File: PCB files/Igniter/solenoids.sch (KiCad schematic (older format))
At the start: 20 parts, among them Q2 N MOSFET, Q3 N MOSFET, Q4 N MOSFET, Q5 N MOSFET, Q6 N MOSFET

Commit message: 10/26/2019
-Added SD card mounting holes
-Added some more footprints
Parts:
- Q2, Q3, Q4, Q5, Q6: footprint (none) -> Package_TO_SOT_THT:TO-220-3_Horizontal_TabDown
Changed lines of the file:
@@
 F 0 "Q4" H 5276 2846 50  0001 L CNN
 F 1 "N MOSFET" H 5276 2800 50  0000 L CNN
-F 2 "" H 5270 2900 50  0001 C CNN
+F 2 "Package_TO_SOT_THT:TO-220-3_Horizontal_TabDown" H 5270 2900 50  0001 C CNN
 F 3 "~" H 5070 2800 50  0001 C CNN
 	1    5070 2800
@@
 F 0 "Q6" H 7386 2876 50  0001 L CNN
 F 1 "N MOSFET" H 7386 2830 50  0000 L CNN
-F 2 "" H 7380 2930 50  0001 C CNN
+F 2 "Package_TO_SOT_THT:TO-220-3_Horizontal_TabDown" H 7380 2930 50  0001 C CNN
 F 3 "~" H 7180 2830 50  0001 C CNN
 	1    7180 2830
@@
 F 0 "Q5" H 7381 4351 50  0001 L CNN
 F 1 "N MOSFET" H 7381 4305 50  0000 L CNN
-F 2 "" H 7375 4405 50  0001 C CNN
+F 2 "Package_TO_SOT_THT:TO-220-3_Horizontal_TabDown" H 7375 4405 50  0001 C CNN
 F 3 "~" H 7175 4305 50  0001 C CNN
 	1    7175 4305
@@
 F 0 "Q3" H 5271 4321 50  0001 L CNN
 F 1 "N MOSFET" H 5271 4275 50  0000 L CNN
-F 2 "" H 5265 4375 50  0001 C CNN
+F 2 "Package_TO_SOT_THT:TO-220-3_Horizontal_TabDown" H 5265 4375 50  0001 C CNN
 F 3 "~" H 5065 4275 50  0001 C CNN
 	1    5065 4275
@@
 F 0 "Q2" H 5246 5871 50  0001 L CNN
 F 1 "N MOSFET" H 5246 5825 50  0000 L CNN
-F 2 "" H 5240 5925 50  0001 C CNN
+F 2 "Package_TO_SOT_THT:TO-220-3_Horizontal_TabDown" H 5240 5925 50  0001 C CNN
 F 3 "~" H 5040 5825 50  0001 C CNN
 	1    5040 5825

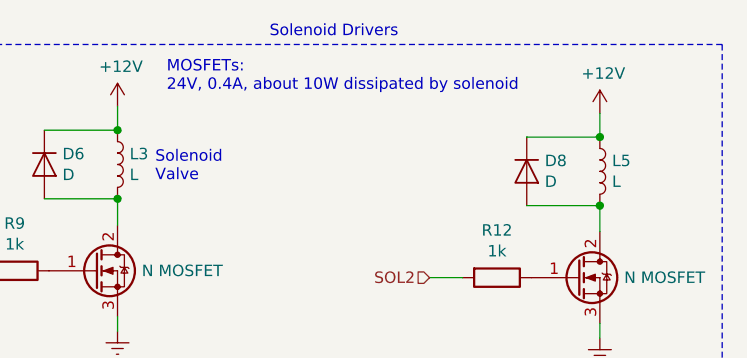
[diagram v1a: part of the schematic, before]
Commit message: 10/27/2019
More 2560 pins named/connected
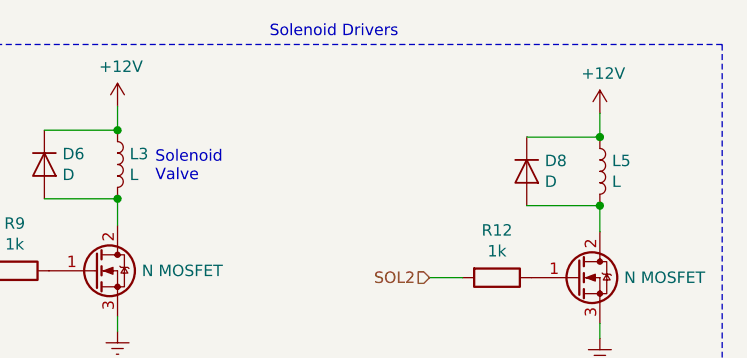
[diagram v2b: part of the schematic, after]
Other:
- note removed: "MOSFETs:\n24V, 0.4A, about 10W dissipated by solenoid\n"
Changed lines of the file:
@@
 LIBS:interface
 LIBS:Igniter-cache
-EELAYER 26 0
+EELAYER 29 0
 EELAYER END
 $Descr A4 11693 8268
@@
 Wire Wire Line
 	7275 4505 7275 4570
-Text Notes 5385 2020 0    50   ~ 0
-MOSFETs:\n24V, 0.4A, about 10W dissipated by solenoid\n
 $Comp
 L Device:Q_NMOS_GDS Q?

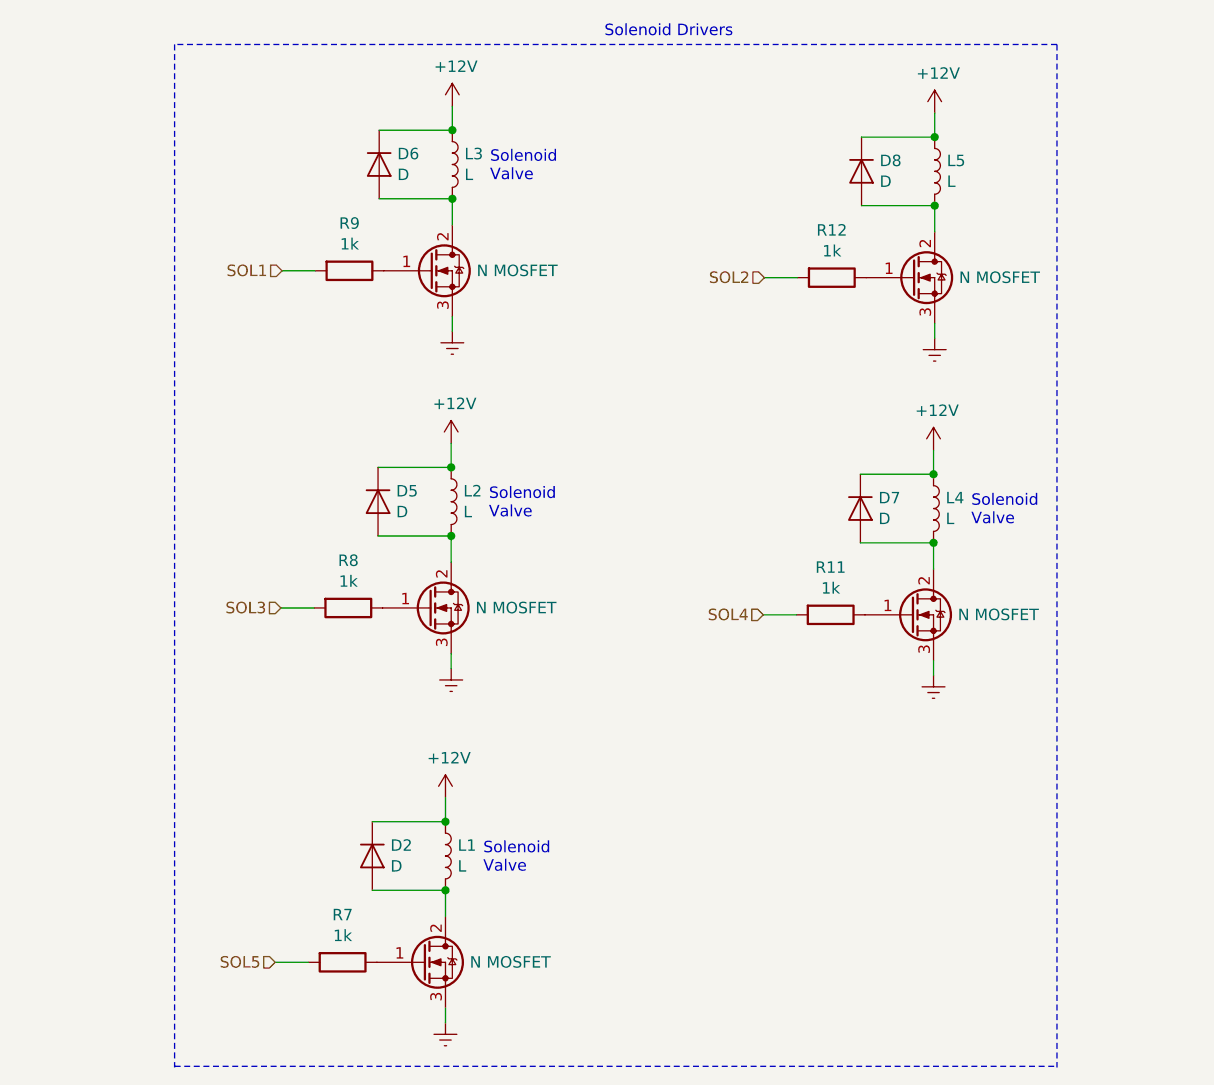
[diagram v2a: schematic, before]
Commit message: 10/30/2019
-Moved keylock
-Removed 1k from MOSFET gates, wasnt adding anything useful to the circuit
-Updated battery voltage to 24V
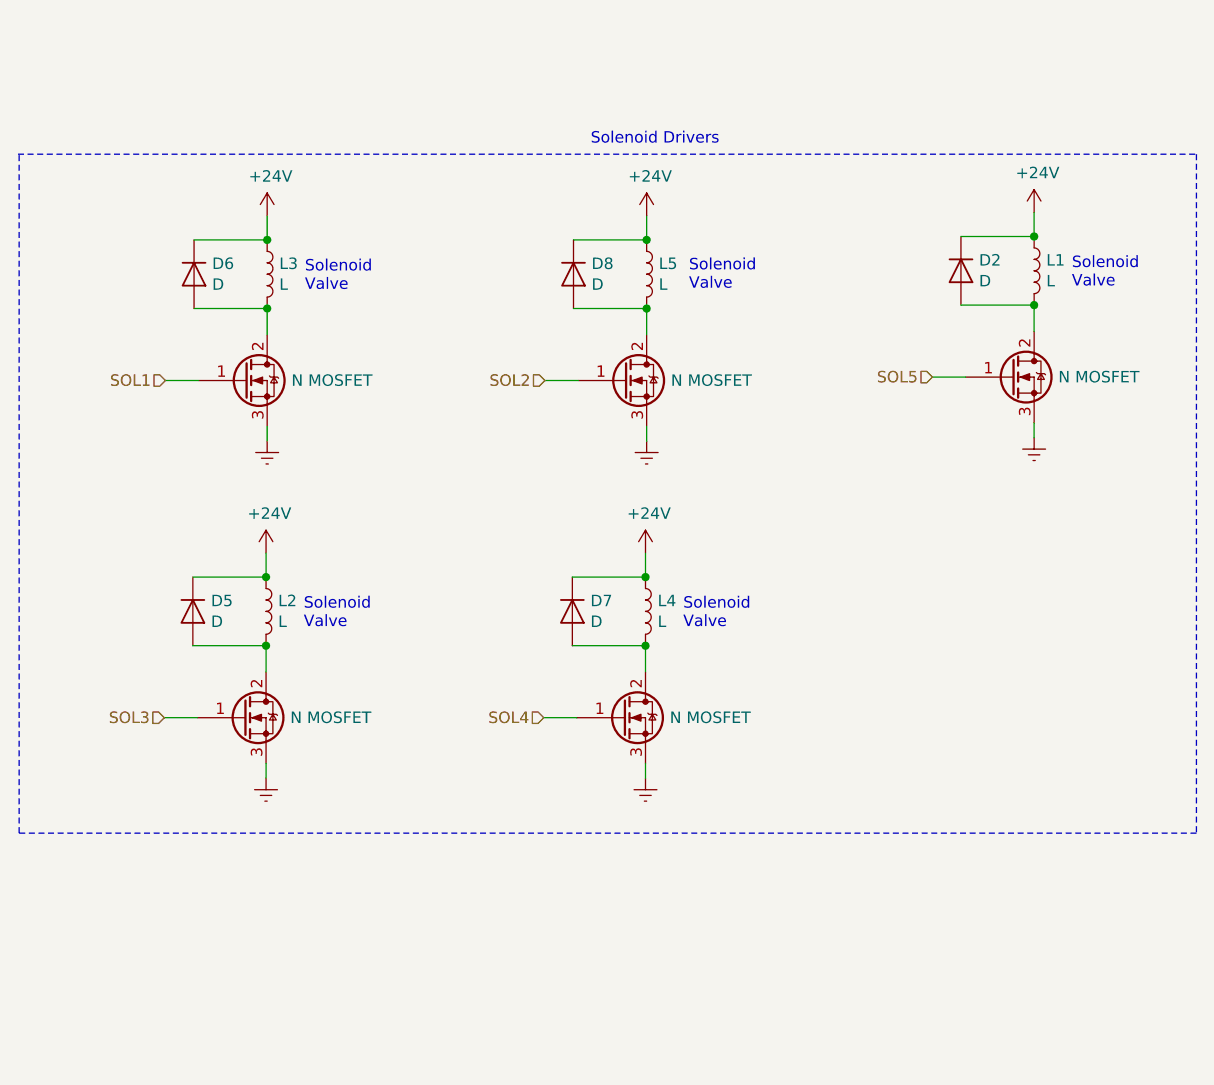
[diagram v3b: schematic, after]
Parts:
- removed R11, R12, R7, R8, R9: 1k, Resistor_THT:R_Axial_DIN0204_L3.6mm_D1.6mm_P5.08mm_Horizontal, symbol Device:R
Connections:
- net SOL1: now also Q4.1 (G)
- net SOL2: now also Q6.1 (G)
- net SOL3: now also Q3.1 (G)
- net SOL4: now also Q5.1 (G)
- net SOL5: now also Q2.1 (G)
- net +12V renamed +24V
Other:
- moved on the sheet: D2, D5, D6, D7, D8, L1, L2, L3, L4, L5

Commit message: 10/31/2019
-Updated and added footprints
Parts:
- D2: footprint (none) -> Diode_THT:D_DO-15_P10.16mm_Horizontal
- D5, D6, D7, D8: footprint (none) -> Diode_THT:D_DO-15_P12.70mm_Horizontal
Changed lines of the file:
@@
 F 0 "D6" V 3994 2894 50  0000 L CNN
 F 1 "D" V 4085 2894 50  0000 L CNN
-F 2 "" H 4040 2815 50  0001 C CNN
+F 2 "Diode_THT:D_DO-15_P12.70mm_Horizontal" H 4040 2815 50  0001 C CNN
 F 3 "~" H 4040 2815 50  0001 C CNN
 	1    4040 2815
@@
 F 0 "D5" V 3989 4369 50  0000 L CNN
 F 1 "D" V 4080 4369 50  0000 L CNN
-F 2 "" H 4035 4290 50  0001 C CNN
+F 2 "Diode_THT:D_DO-15_P12.70mm_Horizontal" H 4035 4290 50  0001 C CNN
 F 3 "~" H 4035 4290 50  0001 C CNN
 	1    4035 4290
@@
 F 0 "D8" V 5654 2894 50  0000 L CNN
 F 1 "D" V 5745 2894 50  0000 L CNN
-F 2 "" H 5700 2815 50  0001 C CNN
+F 2 "Diode_THT:D_DO-15_P12.70mm_Horizontal" H 5700 2815 50  0001 C CNN
 F 3 "~" H 5700 2815 50  0001 C CNN
 	1    5700 2815
@@
 F 0 "D7" V 5649 4369 50  0000 L CNN
 F 1 "D" V 5740 4369 50  0000 L CNN
-F 2 "" H 5695 4290 50  0001 C CNN
+F 2 "Diode_THT:D_DO-15_P12.70mm_Horizontal" H 5695 4290 50  0001 C CNN
 F 3 "~" H 5695 4290 50  0001 C CNN
 	1    5695 4290
@@
 F 0 "D2" V 7349 2879 50  0000 L CNN
 F 1 "D" V 7440 2879 50  0000 L CNN
-F 2 "" H 7395 2800 50  0001 C CNN
+F 2 "Diode_THT:D_DO-15_P10.16mm_Horizontal" H 7395 2800 50  0001 C CNN
 F 3 "~" H 7395 2800 50  0001 C CNN
 	1    7395 2800
@@
 SOL5
 $Comp
-L power:+24V #PWR?
+L power:+24V #PWR0115
 U 1 1 5DBB6885
 P 4360 2560
-F 0 "#PWR?" H 4360 2410 50  0001 C CNN
+F 0 "#PWR0115" H 4360 2410 50  0001 C CNN
 F 1 "+24V" H 4375 2733 50  0000 C CNN
 F 2 "" H 4360 2560 50  0001 C CNN
@@
 $EndComp
 $Comp
-L power:+24V #PWR?
+L power:+24V #PWR0118
 U 1 1 5DBB6A3C
 P 6020 2560
-F 0 "#PWR?" H 6020 2410 50  0001 C CNN
+F 0 "#PWR0118" H 6020 2410 50  0001 C CNN
 F 1 "+24V" H 6035 2733 50  0000 C CNN
 F 2 "" H 6020 2560 50  0001 C CNN
@@
 $EndComp
 $Comp
-L power:+24V #PWR?
+L power:+24V #PWR0119
 U 1 1 5DBB6B6A
 P 7715 2545
-F 0 "#PWR?" H 7715 2395 50  0001 C CNN
+F 0 "#PWR0119" H 7715 2395 50  0001 C CNN
 F 1 "+24V" H 7730 2718 50  0000 C CNN
 F 2 "" H 7715 2545 50  0001 C CNN
@@
 $EndComp
 $Comp
-L power:+24V #PWR?
+L power:+24V #PWR0120
 U 1 1 5DBB6F27
 P 4355 4035
-F 0 "#PWR?" H 4355 3885 50  0001 C CNN
+F 0 "#PWR0120" H 4355 3885 50  0001 C CNN
 F 1 "+24V" H 4370 4208 50  0000 C CNN
 F 2 "" H 4355 4035 50  0001 C CNN
@@
 $EndComp
 $Comp
-L power:+24V #PWR?
+L power:+24V #PWR0121
 U 1 1 5DBB7018
 P 6015 4035
-F 0 "#PWR?" H 6015 3885 50  0001 C CNN
+F 0 "#PWR0121" H 6015 3885 50  0001 C CNN
 F 1 "+24V" H 6030 4208 50  0000 C CNN
 F 2 "" H 6015 4035 50  0001 C CNN
